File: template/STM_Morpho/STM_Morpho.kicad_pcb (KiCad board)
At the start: 2 copper layers, 70 x 59 mm, 2 parts, among them CN10 CONN_02X19, CN7 CONN_02X19

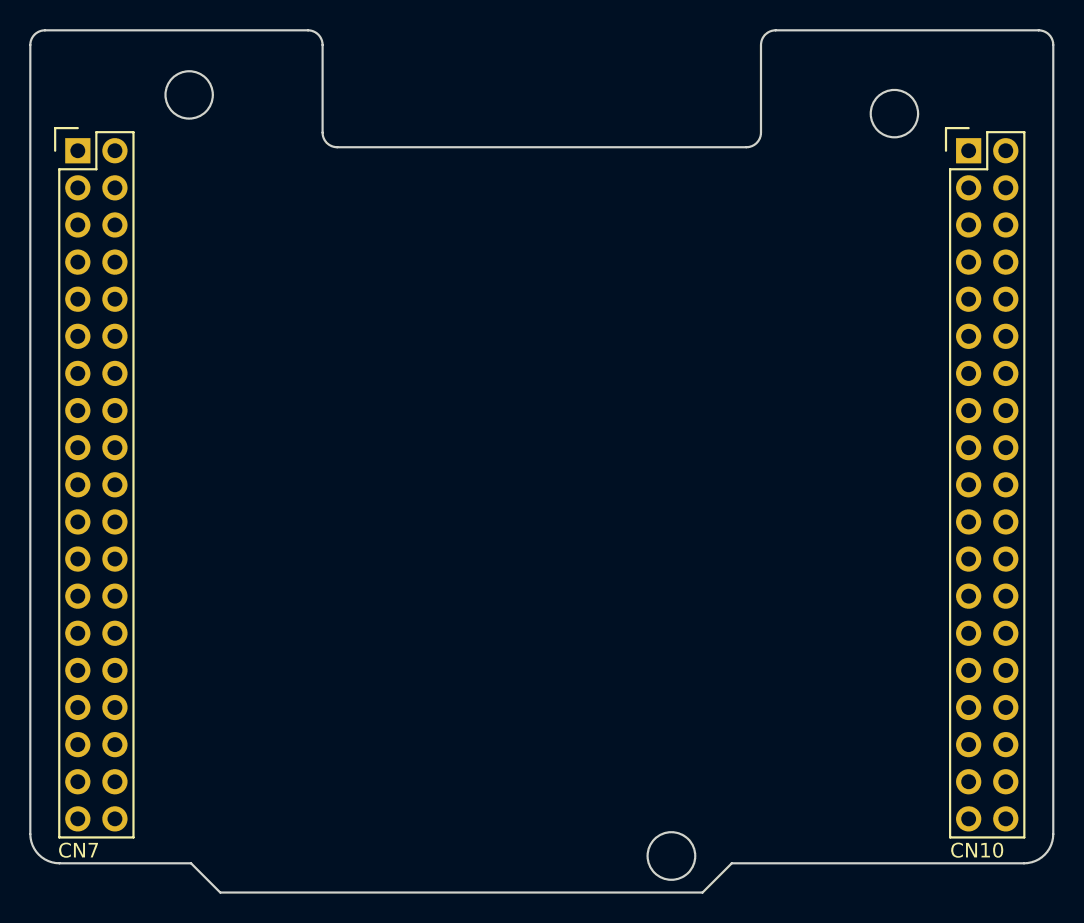
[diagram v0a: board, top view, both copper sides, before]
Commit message: Update for KiCaD 5.1.7
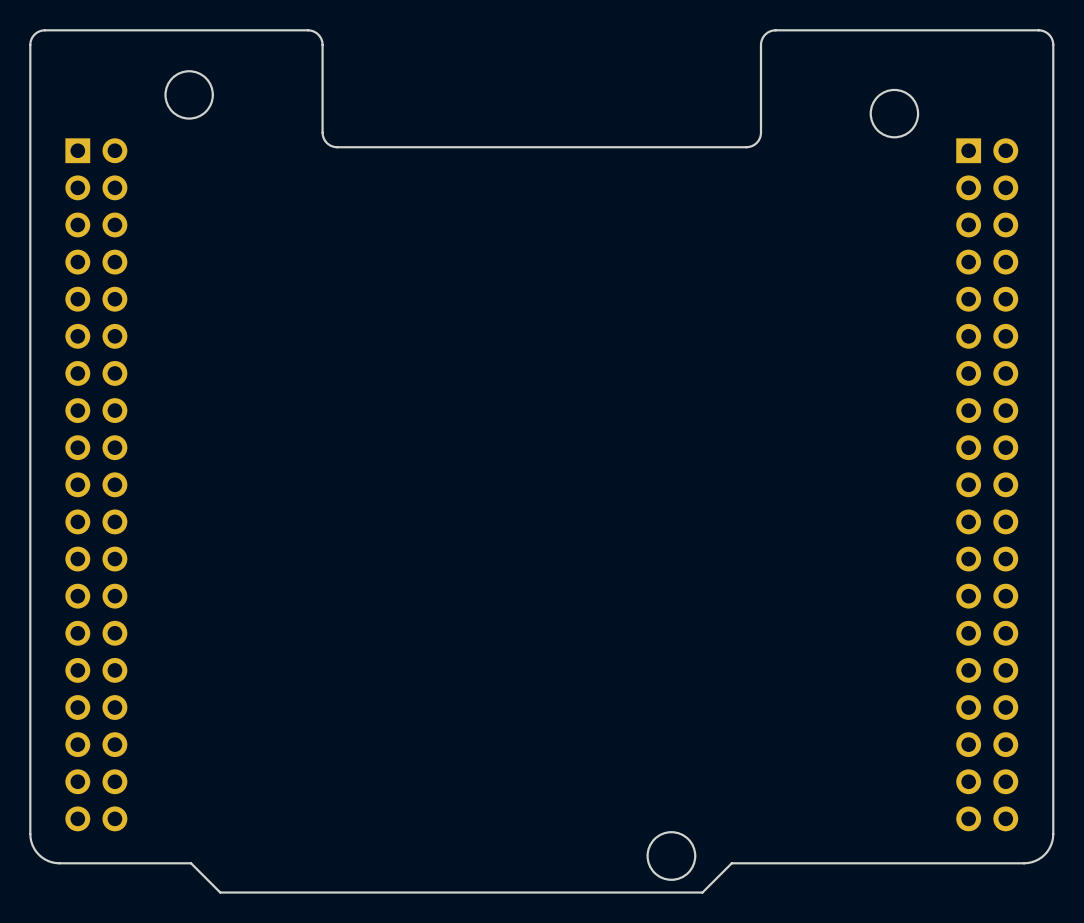
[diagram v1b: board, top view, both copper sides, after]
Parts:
- CN10, CN7: value CONN_02X19 -> Conn_02x19_Odd_Even; footprint Pin_Headers:Pin_Header_Straight_2x19 -> Connector_PinSocket_2.54mm:PinSocket_2x19_P2.54mm_Vertical; moved to B.Cu
- turned CN10 to 180 degrees
- turned CN7 to 180 degrees
